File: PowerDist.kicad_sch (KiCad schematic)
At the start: 21 parts, among them U1 TPS2121RUXR

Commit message: BOM
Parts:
- C2, C3, C4: P/N (none) -> C0805C104M5RACTU
- C5: P/N (none) -> C0805C105K5PACTU
- R12, R6, R7: P/N (none) -> CRCW08055K00FKTA
- R13: P/N (none) -> CRCW080551K0FKEA
- R4: P/N (none) -> CRCW0805100KFKEAC
- R5, R8: P/N (none) -> CRCW080562K0FKEA
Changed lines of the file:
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@@
+			)
+		)
+		(property "P/N" "C0805C105K5PACTU"
+			(at 57.15 72.39 0)
+			(effects
+				(font
+					(size 1.27 1.27)
+				)
+				(hide yes)
 			)
 		)
@@
 			)
 		)
+		(property "P/N" "CRCW08055K00FKTA"
+			(at 172.72 74.93 0)
+			(effects
+				(font
+					(size 1.27 1.27)
+				)
+				(hide yes)
+			)
+		)
 		(pin "2"
 		)
@@
 			)
 		)
+		(property "P/N" "CRCW08055K00FKTA"
+			(at 119.38 101.6 0)
+			(effects
+				(font
+					(size 1.27 1.27)
+				)
+				(hide yes)
+			)
+		)
 		(pin "2"
 		)
@@
 			)
 		)
+		(property "P/N" "CRCW080551K0FKEA"
+			(at 92.71 60.96 0)
+			(effects
+				(font
+					(size 1.27 1.27)
+				)
+				(hide yes)
+			)
+		)
 		(pin "2"
 		)
@@
 			)
 		)
+		(property "P/N" "CRCW080562K0FKEA"
+			(at 119.38 88.9 0)
+			(effects
+				(font
+					(size 1.27 1.27)
+				)
+				(hide yes)
+			)
+		)
 		(pin "2"
 		)
@@
 			)
 		)
+		(property "P/N" "C0805C104M5RACTU"
+			(at 179.07 87.63 0)
+			(effects
+				(font
+					(size 1.27 1.27)
+				)
+				(hide yes)
+			)
+		)
 		(pin "2"
 		)
@@
 		)
 		(property "Description" "Unpolarized capacitor"
+			(at 26.67 72.39 0)
+			(effects
+				(font
+					(size 1.27 1.27)
+				)
+				(hide yes)
+			)
+		)
+		(property "P/N" "C0805C104M5RACTU"
 			(at 26.67 72.39 0)
 			(effects
@@
 			)
 		)
+		(property "P/N" "C0805C104M5RACTU"
+			(at 41.91 72.39 0)
+			(effects
+				(font
+					(size 1.27 1.27)
+				)
+				(hide yes)
+			)
+		)
 		(pin "2"
 		)
@@
 			)
 		)
+		(property "P/N" "CRCW0805100KFKEAC"
+			(at 163.83 90.17 0)
+			(effects
+				(font
+					(size 1.27 1.27)
+				)
+				(hide yes)
+			)
+		)
 		(pin "2"
 		)
@@
 			)
 		)
+		(property "P/N" "CRCW08055K00FKTA"
+			(at 92.71 73.66 0)
+			(effects
+				(font
+					(size 1.27 1.27)
+				)
+				(hide yes)
+			)
+		)
 		(pin "2"
 		)
@@
 			(at 172.72 60.96 0)
 			(effects
+				(font
+					(size 1.27 1.27)
+				)
+				(hide yes)
+			)
+		)
+		(property "P/N" "CRCW080562K0FKEA"
+			(at 172.72 60.96 0)
+			(effects

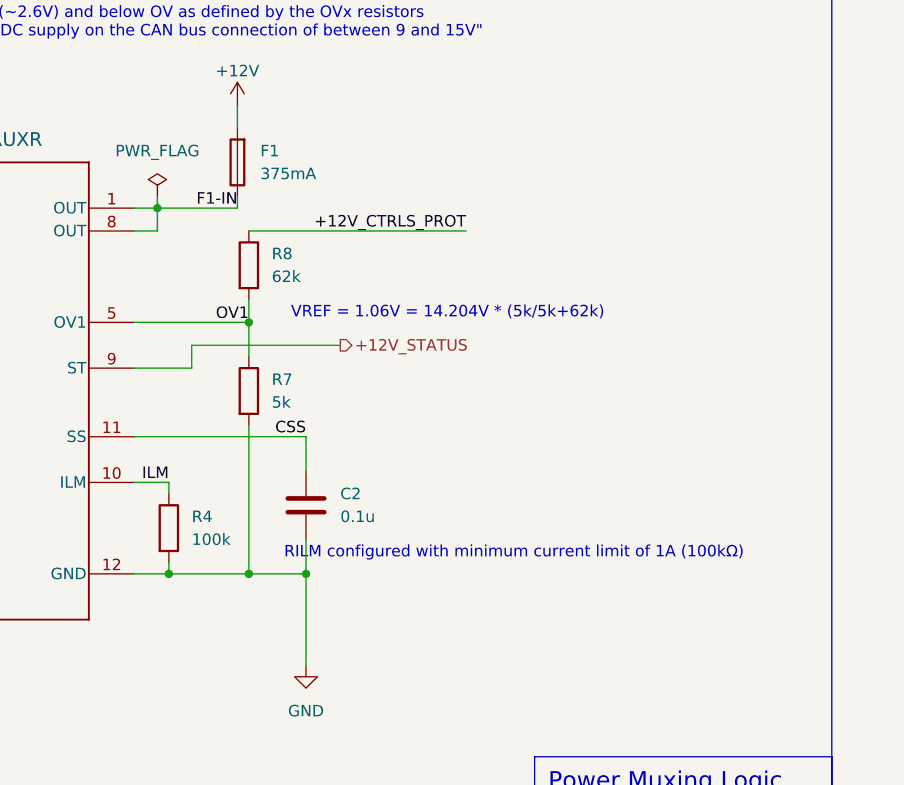
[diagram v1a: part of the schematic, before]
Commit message: add fan conns, layout + routing
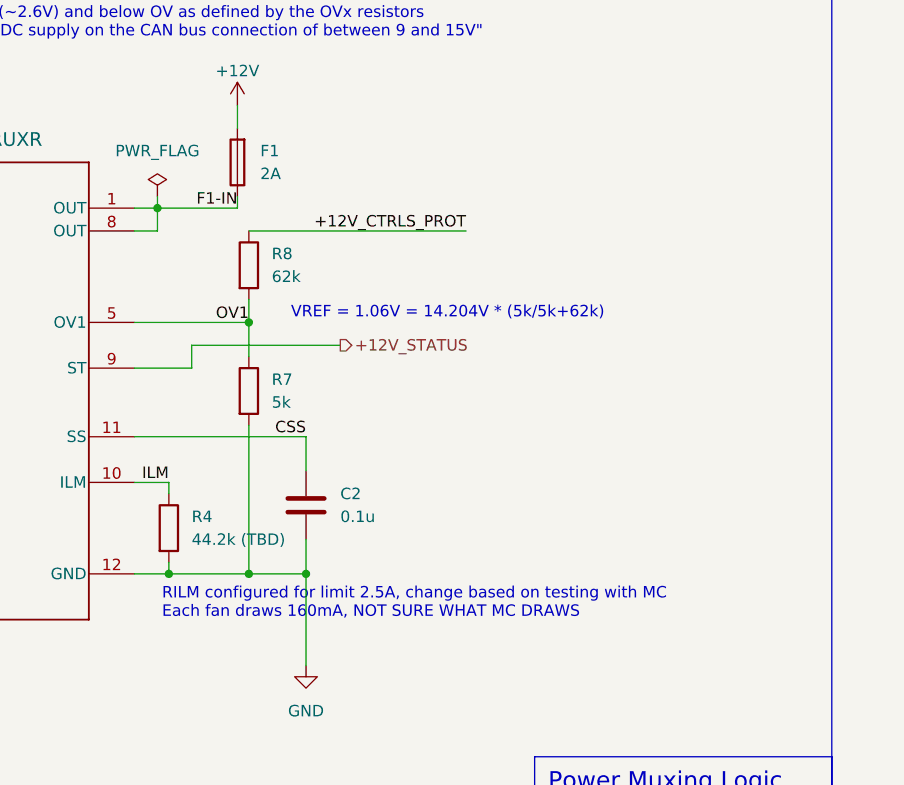
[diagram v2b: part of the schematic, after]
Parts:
- F1: value 375mA -> 2A; Mouser Part Number 576-0440.375WR -> 576-0440002.WR; P/N 576-0440.375WR -> 0440002.WR
- R4: value 100k -> 44.2k (TBD); P/N CRCW0805100KFKEAC -> TBD
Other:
- note added: "RILM configured for limit 2.5A, change based on testing with MC Each fan draws 160mA, NOT SURE WHAT MC DRAWS"
- note removed: "RILM configured with minimum current limit of 1A (100kΩ)"
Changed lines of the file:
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@@
 		)
 	)
-	(text "RILM configured with minimum current limit of 1A (100kΩ)"
-		(exclude_from_sim no)
-		(at 202.184 92.964 0)
-		(effects
-			(font
-				(size 1.27 1.27)
-			)
+	(text "RILM configured for limit 2.5A, change based on testing with MC\nEach fan draws 160mA, NOT SURE WHAT MC DRAWS"
+		(exclude_from_sim no)
+		(at 163.068 98.552 0)
+		(effects
+			(font
+				(size 1.27 1.27)
+			)
+			(justify left)
 		)
 	)
@@
 			)
 		)
-		(property "Value" "375mA"
+		(property "Value" "2A"
 			(at 173.99 50.7999 0)
 			(effects
@@
 			)
 		)
-		(property "Mouser Part Number" "576-0440.375WR"
+		(property "Mouser Part Number" "576-0440002.WR "
 			(at 171.45 49.53 0)
 			(effects
@@
 			)
 		)
-		(property "P/N" "576-0440.375WR "
+		(property "P/N" "0440002.WR "
 			(at 171.45 49.53 0)
 			(effects
@@
 			)
 		)
-		(property "Value" "100k"
+		(property "Value" "44.2k (TBD)"
 			(at 166.37 91.4399 0)
 			(effects
@@
 			)
 		)
-		(property "P/N" "CRCW0805100KFKEAC"
+		(property "P/N" "TBD"
 			(at 163.83 90.17 0)
 			(effects
